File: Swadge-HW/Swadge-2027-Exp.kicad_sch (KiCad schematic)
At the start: 4 parts, among them U15 GD25Q32ES

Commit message: Bus Renames
Since we really don't have that many signals I just ditched the bus prefixes and Alias'd them directly.
Added a bus for the interupt and status signals even if they are never used.
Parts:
- U15: now not fitted; now left out of the parts list
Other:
- note added: "EXPANSION SLOT - SPI2 bus with CS1 Available to be populated with more flash ram"
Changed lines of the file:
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@@
 		(company "Magfest Inc")
+	)
+	(text "EXPANSION SLOT -\nSPI2 bus with CS1\nAvailable to be populated with\nmore flash ram"
+		(exclude_from_sim no)
+		(at 149.86 48.26 0)
+		(effects
+			(font
+				(size 1.27 1.27)
+			)
+		)
 	)
 	(junction
@@
 		)
 	)
-	(hierarchical_label "COMM{COMM_BUS}"
+	(hierarchical_label "{COMM}"
 		(shape bidirectional)
 		(at 119.38 73.66 180)
@@
 		(body_style 1)
 		(exclude_from_sim no)
-		(in_bom yes)
+		(in_bom no)
 		(on_board yes)
 		(in_pos_files yes)
-		(dnp no)
+		(dnp yes)
 		(fields_autoplaced yes)
 		(property "Reference" "U15"

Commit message: Annotations
Updated Annotations with zonal numbering
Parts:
- renumbered C38 to C81, R39 to R81, R38 to R82, U15 to U8
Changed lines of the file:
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@@
 		(in_pos_files yes)
 		(dnp no)
-		(property "Reference" "R39"
+		(property "Reference" "R81"
 			(at 104.14 85.09 90)
 			(show_name no)
@@
 			(project "Swadge-HW"
 				(path "/770c762f-3a30-4864-b7da-de353459cdd6/34139379-2635-49cf-a6ce-849443f55915"
-					(reference "R39")
+					(reference "R81")
 					(unit 1)
 				)
@@
 		(in_pos_files yes)
 		(dnp no)
-		(property "Reference" "R38"
+		(property "Reference" "R82"
 			(at 93.98 85.09 90)
 			(show_name no)
@@
 			(project "Swadge-HW"
 				(path "/770c762f-3a30-4864-b7da-de353459cdd6/34139379-2635-49cf-a6ce-849443f55915"
-					(reference "R38")
+					(reference "R82")
 					(unit 1)
 				)
@@
 		(dnp yes)
 		(fields_autoplaced yes)
-		(property "Reference" "U15"
+		(property "Reference" "U8"
 			(at 160.782 95.3078 0)
 			(show_name no)
@@
 			(project "Swadge-HW"
 				(path "/770c762f-3a30-4864-b7da-de353459cdd6/34139379-2635-49cf-a6ce-849443f55915"
-					(reference "U15")
+					(reference "U8")
 					(unit 1)
 				)
@@
 		(in_pos_files yes)
 		(dnp no)
-		(property "Reference" "C38"
+		(property "Reference" "C81"
 			(at 170.815 74.93 0)
 			(show_name no)
@@
 			(project "Swadge-HW"
 				(path "/770c762f-3a30-4864-b7da-de353459cdd6/34139379-2635-49cf-a6ce-849443f55915"
-					(reference "C38")
+					(reference "C81")
 					(unit 1)
 				)

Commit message: major routing changes
Routed SPI
Started Test Routing Touch Inputs
Rough routing for LCD Power
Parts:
- C81: Cost @ 2.5k 0.0015 -> 0.0182; LCSC C282519 -> C14663
- R81, R82: Cost @ 2.5k 0.0007 -> 0.0037; LCSC C25804 -> C2906982
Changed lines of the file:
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@@
 			)
 		)
-		(property "LCSC" "C25804"
+		(property "LCSC" "C2906982"
 			(at 101.6 85.09 0)
 			(hide yes)
@@
 			)
 		)
-		(property "Cost @ 2.5k" "0.0007"
+		(property "Cost @ 2.5k" "0.0037"
 			(at 101.6 85.09 0)
 			(hide yes)
@@
 			)
 		)
-		(property "LCSC" "C25804"
-			(at 91.44 85.09 0)
-			(hide yes)
-			(show_name no)
-			(do_not_autoplace no)
-			(effects
-				(font
-					(size 1.27 1.27)
-				)
-			)
-		)
-		(property "Cost @ 2.5k" "0.0007"
+		(property "LCSC" "C2906982"
+			(at 91.44 85.09 0)
+			(hide yes)
+			(show_name no)
+			(do_not_autoplace no)
+			(effects
+				(font
+					(size 1.27 1.27)
+				)
+			)
+		)
+		(property "Cost @ 2.5k" "0.0037"
 			(at 91.44 85.09 0)
 			(hide yes)
@@
 			)
 		)
-		(property "LCSC" "C282519"
-			(at 170.18 77.47 0)
-			(hide yes)
-			(show_name no)
-			(do_not_autoplace no)
-			(effects
-				(font
-					(size 1.27 1.27)
-				)
-			)
-		)
-		(property "Cost @ 2.5k" "0.0015"
-			(at 170.18 77.47 0)
-			(hide yes)
+		(property "LCSC" "C14663"
+			(at 170.18 77.47 0)
+			(hide yes)
+			(show_name no)
+			(do_not_autoplace no)
+			(effects
+				(font
+					(size 1.27 1.27)
+				)
+			)
+		)
+		(property "Cost @ 2.5k" "0.0182"
+			(at 170.18 77.47 0)
+			(hide yes)

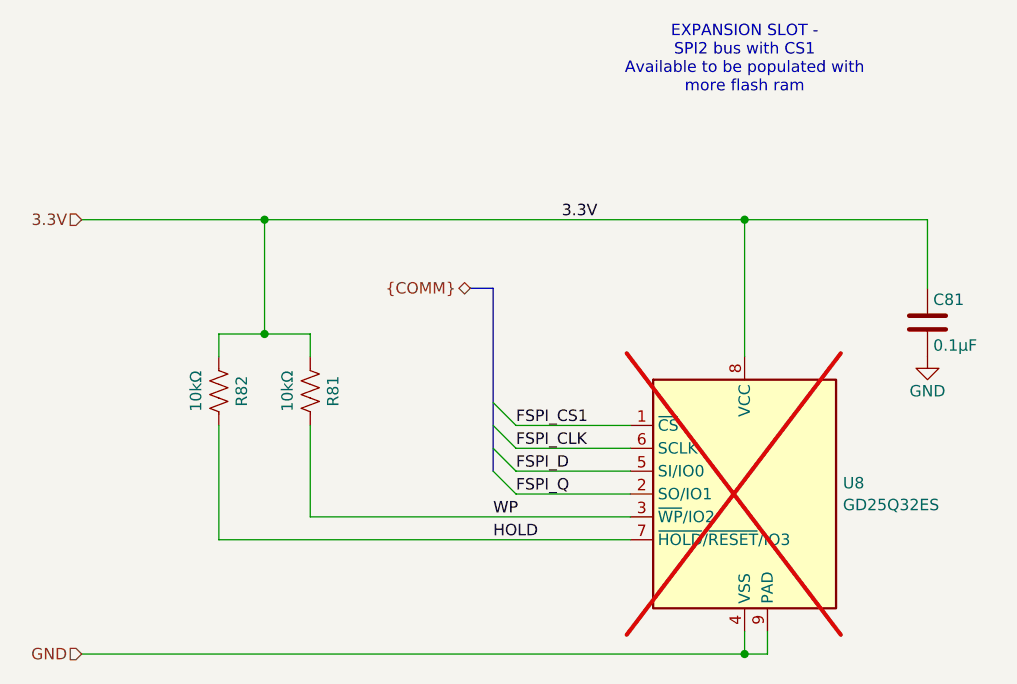
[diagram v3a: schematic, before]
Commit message: Change to ESP32-S3-MINI-1
Change U1 to ESP32-S3-MINI-1-N4R2
Update IO Mapping
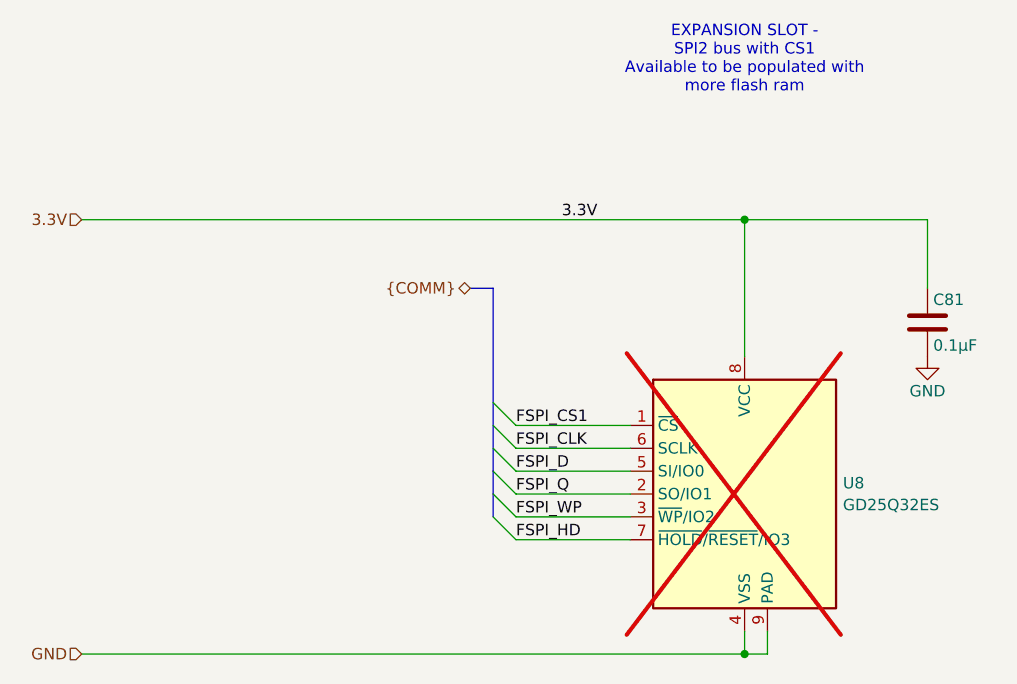
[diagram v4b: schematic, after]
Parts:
- removed R81, R82: 10kΩ, Swadge_Parts:R_0603_1608Metric, symbol Swadge_Parts:R_US
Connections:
- net HOLD renamed FSPI_HD
- net WP renamed FSPI_WP
